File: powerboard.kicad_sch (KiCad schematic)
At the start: 24 parts, among them J1 B03B, J2 EMER_SW, J3 EMER_SW, Q1 TJ60S04M3L, U1 TLP222A

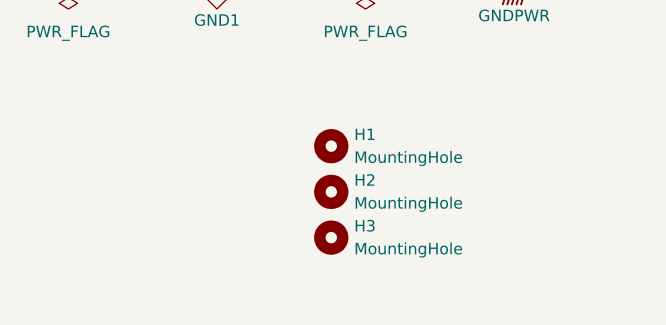
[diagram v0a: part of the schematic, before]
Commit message: pcb/sch: add a hole, silks
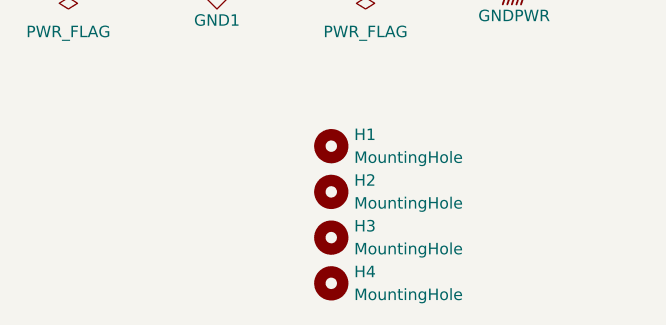
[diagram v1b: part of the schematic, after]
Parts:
- added H4: MountingHole, MountingHole:MountingHole_3.2mm_M3, symbol Mechanical:MountingHole
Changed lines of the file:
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@@
+	)
+	(symbol
+		(lib_id "Mechanical:MountingHole")
+		(at 248.92 100.33 0)
+		(unit 1)
+		(exclude_from_sim yes)
+		(in_bom no)
+		(on_board yes)
+		(dnp no)
+		(fields_autoplaced yes)
+		(property "Reference" "H4"
+			(at 251.46 99.0599 0)
+			(effects
+				(font
+					(size 1.27 1.27)
+				)
+				(justify left)
+			)
+		)
+		(property "Value" "MountingHole"
+			(at 251.46 101.5999 0)
+			(effects
+				(font
+					(size 1.27 1.27)
+				)
+				(justify left)
+			)
+		)
+		(property "Footprint" "MountingHole:MountingHole_3.2mm_M3"
+			(at 248.92 100.33 0)
+			(effects
+				(font
+					(size 1.27 1.27)
+				)
+				(hide yes)
+			)
+		)
+		(property "Datasheet" "~"
+			(at 248.92 100.33 0)
+			(effects
+				(font
+					(size 1.27 1.27)
+				)
+				(hide yes)
+			)
+		)
+		(property "Description" "Mounting Hole without connection"
+			(at 248.92 100.33 0)
+			(effects
+				(font
+					(size 1.27 1.27)
+				)
+				(hide yes)
+			)
+		)
+		(instances
+			(project "powerboard"
+				(path "/f61afb78-be8f-4a5f-ad16-61c0881e4198"
+					(reference "H4")
+					(unit 1)
+				)
+			)
+		)
 	)
 	(symbol

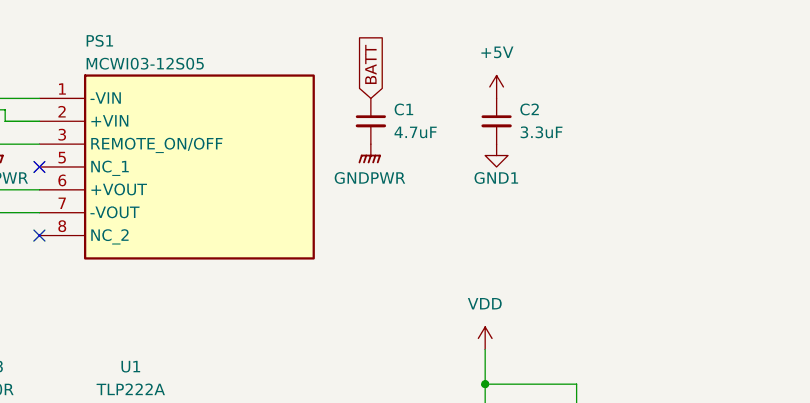
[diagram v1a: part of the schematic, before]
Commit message: sch: change Capacitance C1 (Power)
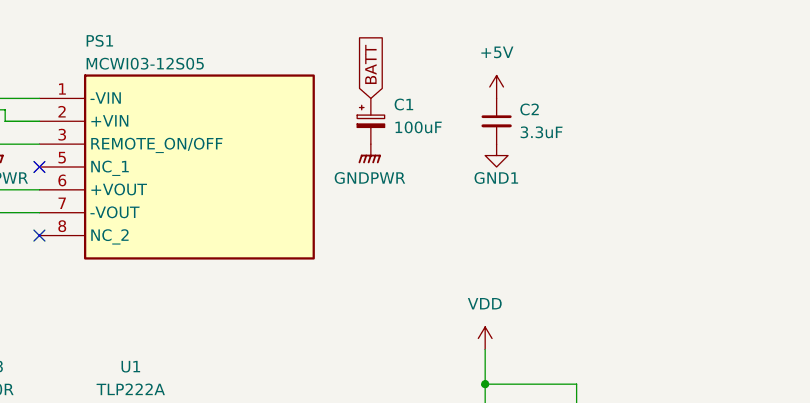
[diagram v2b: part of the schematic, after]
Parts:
- C1: value 4.7uF -> 100uF; footprint Capacitor_THT:C_Disc_D5.1mm_W3.2mm_P5.00mm -> Capacitor_THT:C_Radial_D5.0mm_H11.0mm_P2.00mm; symbol Device:C_Small -> Device:C_Polarized_Small
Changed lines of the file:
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@@
 	)
 	(symbol
-		(lib_id "Device:C_Small")
+		(lib_id "Device:C_Polarized_Small")
 		(at 132.08 36.83 0)
 		(unit 1)
@@
 		(fields_autoplaced yes)
 		(property "Reference" "C1"
-			(at 134.62 35.5662 0)
+			(at 134.62 35.0138 0)
 			(effects
 				(font
@@
 			)
 		)
-		(property "Value" "4.7uF"
-			(at 134.62 38.1062 0)
+		(property "Value" "100uF"
+			(at 134.62 37.5538 0)
 			(effects
 				(font
@@
 			)
 		)
-		(property "Footprint" "Capacitor_THT:C_Disc_D5.1mm_W3.2mm_P5.00mm"
+		(property "Footprint" "Capacitor_THT:C_Radial_D5.0mm_H11.0mm_P2.00mm"
 			(at 132.08 36.83 0)
 			(effects
@@
 			)
 		)
-		(property "Description" "Unpolarized capacitor, small symbol"
+		(property "Description" "Polarized capacitor, small symbol"
 			(at 132.08 36.83 0)
 			(effects

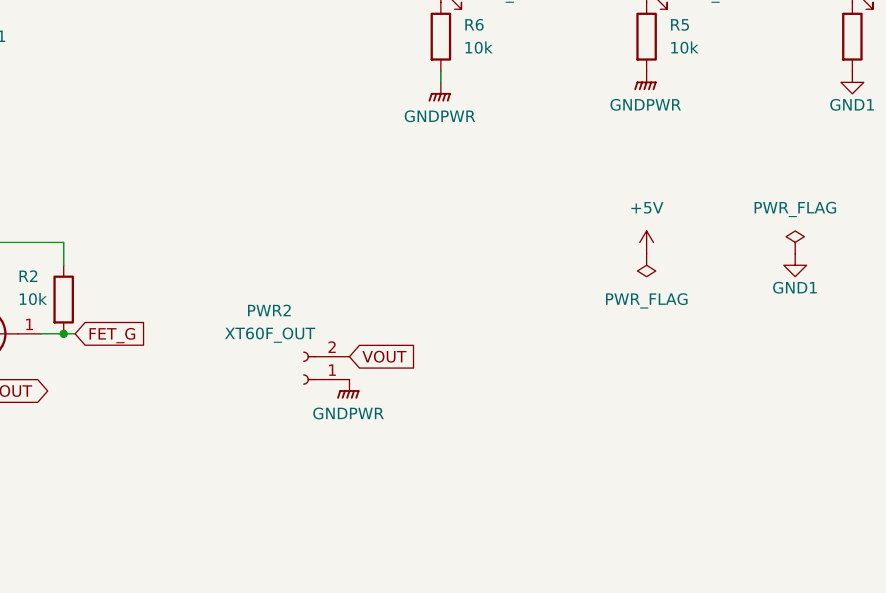
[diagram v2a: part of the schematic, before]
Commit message: pcb/sch: Add FET
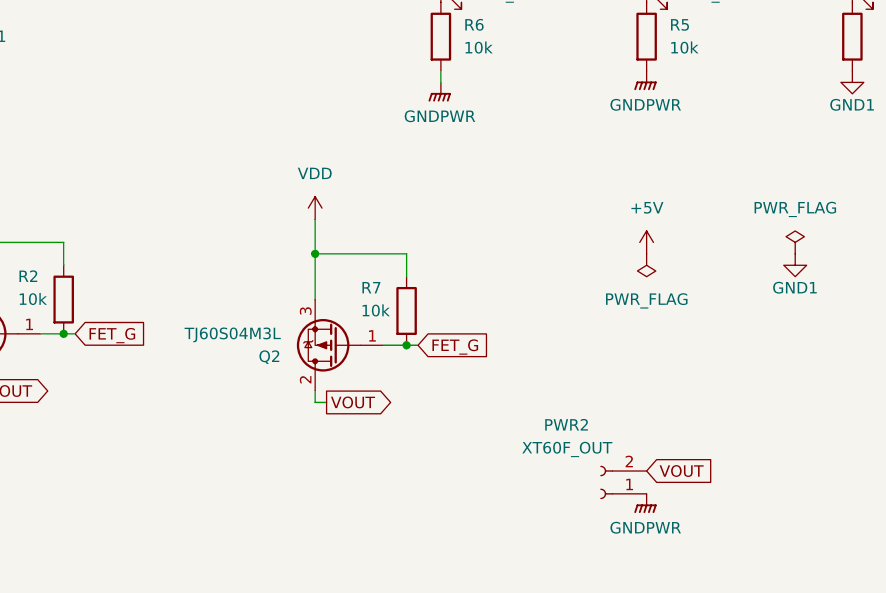
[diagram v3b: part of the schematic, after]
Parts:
- added Q2: TJ60S04M3L, Package_TO_SOT_SMD:TO-252-2, symbol Device:Q_PMOS_GDS
- added R7: 10k, Resistor_THT:R_Axial_DIN0207_L6.3mm_D2.5mm_P7.62mm_Horizontal, symbol Device:R
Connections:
- net FET_G: now also Q2.1 (G), R7.2
- net VDD: now also Q2.3 (S), R7.1
- net VOUT: now also Q2.2 (D)
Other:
- moved on the sheet: PWR2

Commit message: Revert "pcb/sch: Add FET"
This reverts commit 0032eebc1d6eb9ed2a957a3795ce5049efafd74e.
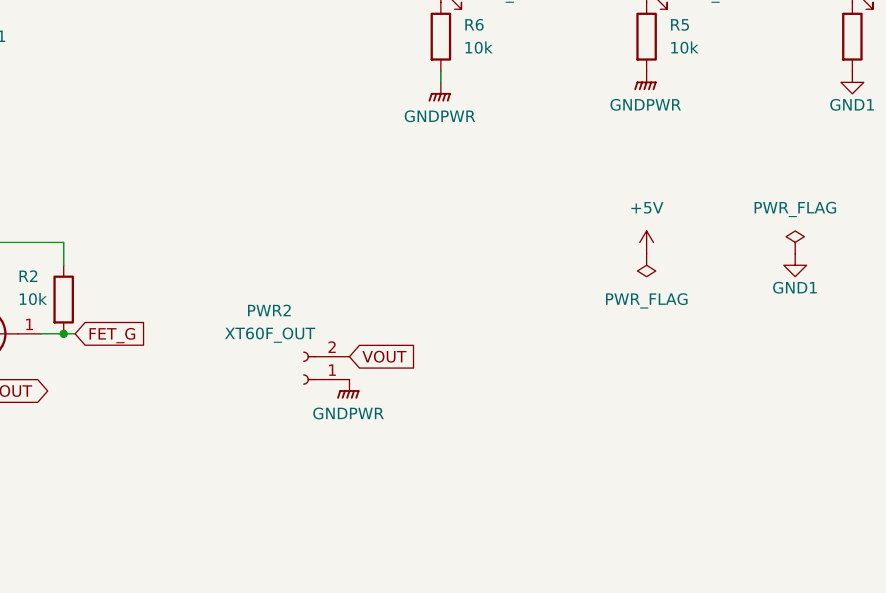
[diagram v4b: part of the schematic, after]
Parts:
- removed Q2: TJ60S04M3L, Package_TO_SOT_SMD:TO-252-2, symbol Device:Q_PMOS_GDS
- removed R7: 10k, Resistor_THT:R_Axial_DIN0207_L6.3mm_D2.5mm_P7.62mm_Horizontal, symbol Device:R
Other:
- moved on the sheet: PWR2

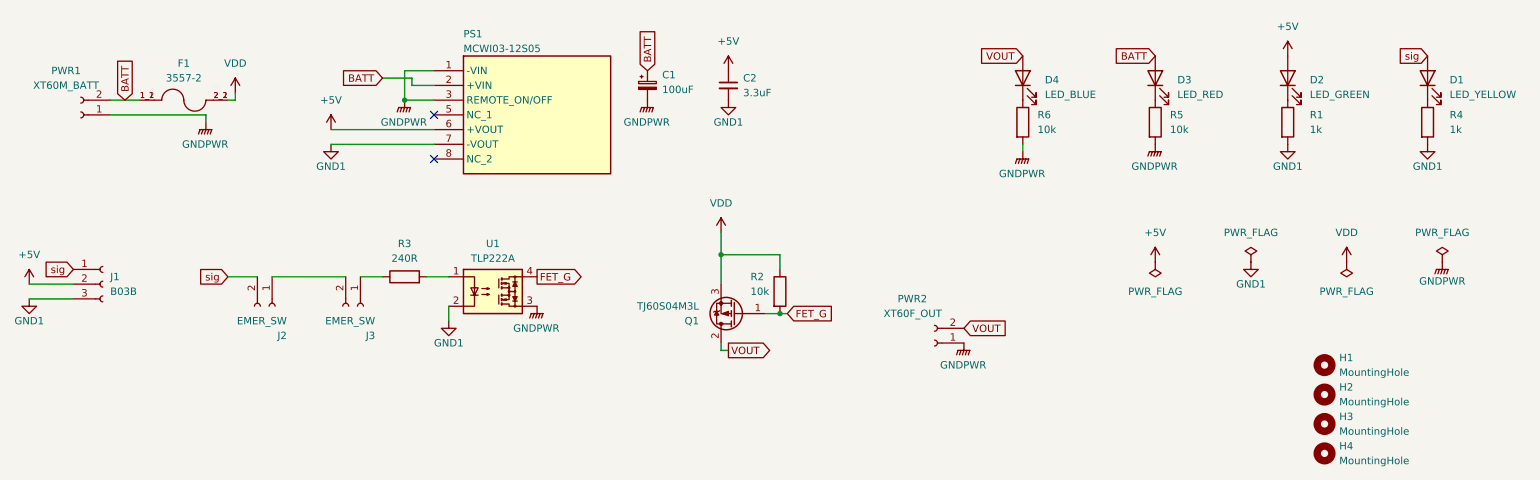
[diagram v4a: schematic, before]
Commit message: PCB: 分圧抵抗を追加、アノテーションをリセット
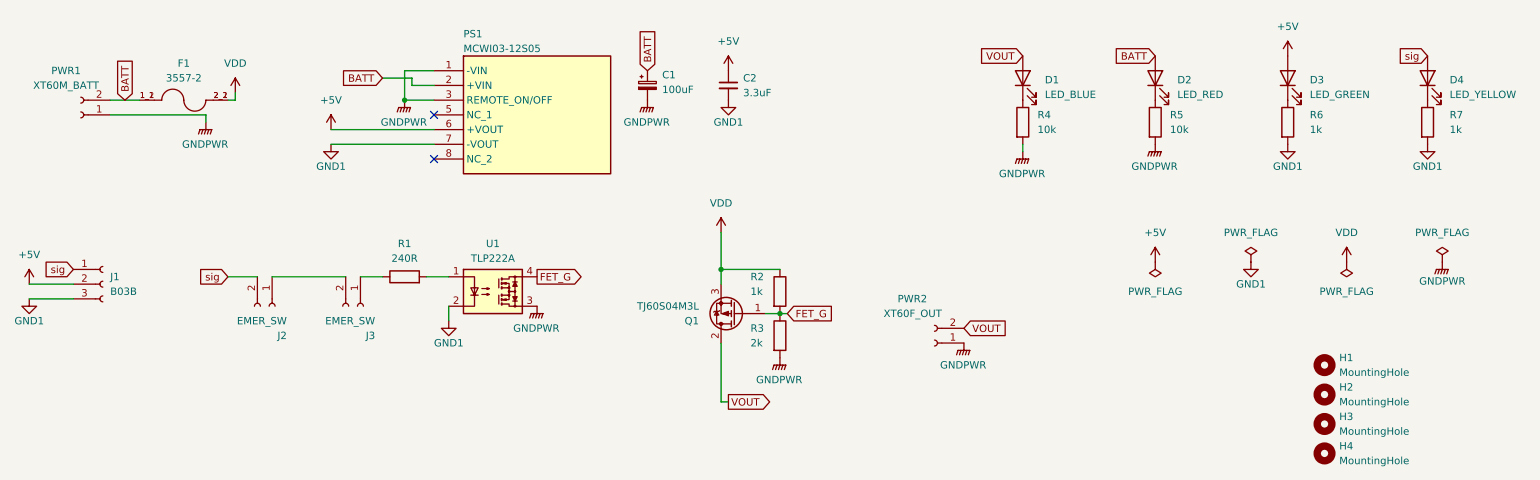
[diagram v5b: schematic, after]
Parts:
- added R3: 2k, symbol Device:R
- R2: value 10k -> 1k
- renumbered D4 to D1, D3 to D2, D2 to D3, D1 to D4, R3 to R1, R6 to R4, R1 to R6, R4 to R7
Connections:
- net FET_G: now also R3.1
- net GNDPWR: now also R3.2

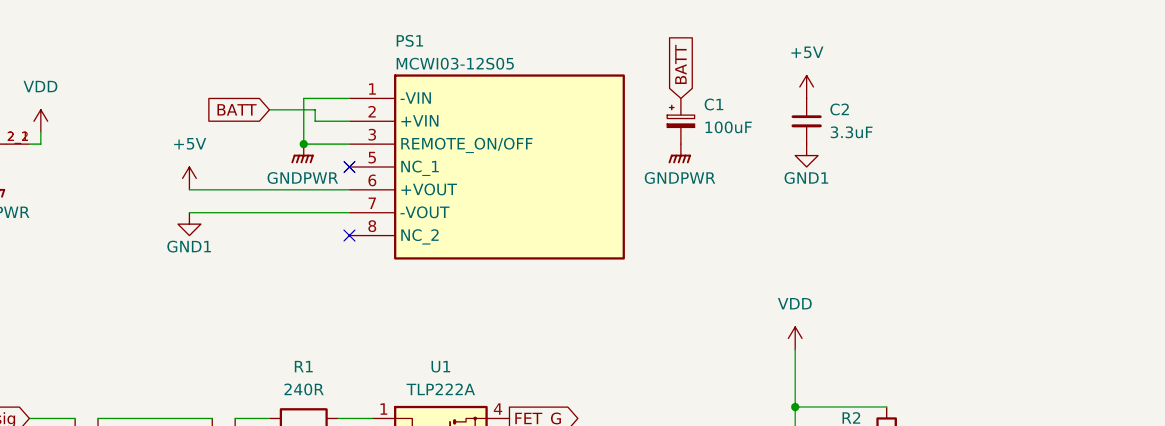
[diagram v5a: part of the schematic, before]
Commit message: PCB: DCDCを変更
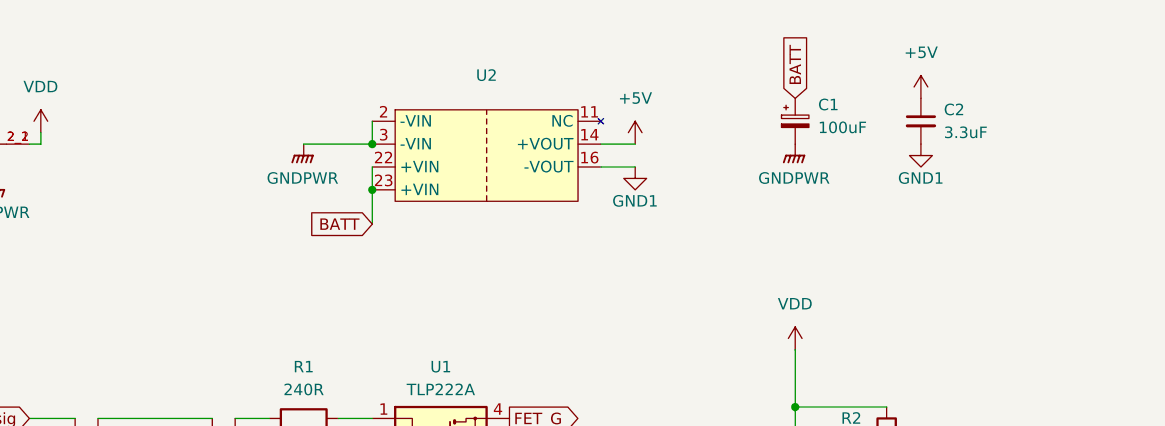
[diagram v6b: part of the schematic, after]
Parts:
- removed PS1: MCWI03-12S05, MCWI0312S05:MCWI0312S05, symbol MCWI03-12S05:MCWI03-12S05
- added U2: ~, symbol MIWI06-24S05:MIWI06-24S05
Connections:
- net +5V: now also U2.14 (+VOUT)
- net BATT: now also U2.22 (+VIN), U2.23 (+VIN)
- net GND1: now also U2.16 (-VOUT)
- net GNDPWR: now also U2.2 (-VIN), U2.3 (-VIN)
- no-connect marks 2 -> 0
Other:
- moved on the sheet: C1, C2

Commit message: PCB: DCDCの位置調整
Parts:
- added R4: 10k, Resistor_THT:R_Axial_DIN0207_L6.3mm_D2.5mm_P7.62mm_Horizontal, symbol Device:R
- R2: value 1k -> 10k
- R3: value 2k -> 10k; footprint (none) -> Resistor_THT:R_Axial_DIN0207_L6.3mm_D2.5mm_P7.62mm_Horizontal
- U1: renamed from U2; footprint (none) -> MIWI06-24S05:MIWI06-24S05
- renumbered R4 to R5, R5 to R6, R6 to R7, R7 to R8, U1 to U2
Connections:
- net GNDPWR: now also R4.2; no longer R3.2
- new net: R3.2, R4.1
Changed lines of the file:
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@@
 	(wire
 		(pts
-			(xy 144.78 91.44) (xy 144.78 81.28)
+			(xy 144.78 83.82) (xy 144.78 81.28)
 		)
 		(stroke
@@
 	(wire
 		(pts
-			(xy 146.05 91.44) (xy 144.78 91.44)
+			(xy 143.51 83.82) (xy 144.78 83.82)
 		)
 		(stroke
@@
 	(global_label "VOUT"
 		(shape output)
-		(at 146.05 91.44 0)
+		(at 143.51 83.82 180)
 		(fields_autoplaced yes)
 		(effects
@@
 				(size 1.27 1.27)
 			)
-			(justify left)
+			(justify right)
 		)
 		(property "Intersheetrefs" "${INTERSHEET_REFS}"
-			(at 153.7524 91.44 0)
+			(at 135.8076 83.82 0)
 			(effects
 				(font
 					(size 1.27 1.27)
 				)
-				(justify left)
+				(justify right)
 				(hide yes)
 			)
@@
 	(symbol
 		(lib_id "power:GNDPWR")
-		(at 154.94 83.82 0)
+		(at 154.94 91.44 0)
 		(unit 1)
 		(exclude_from_sim no)
@@
 		(dnp no)
 		(fields_autoplaced yes)
-		(property "Reference" "#PWR014"
-			(at 154.94 88.9 0)
+		(property "Reference" "#PWR012"
+			(at 154.94 96.52 0)
 			(effects
 				(font
@@
 		)
 		(property "Value" "GNDPWR"
-			(at 154.813 87.63 0)
+			(at 154.813 95.25 0)
 			(effects
 				(font
@@
 		)
 		(property "Footprint" ""
-			(at 154.94 85.09 0)
+			(at 154.94 92.71 0)
 			(effects
 				(font
@@
 		)
 		(property "Datasheet" ""
-			(at 154.94 85.09 0)
+			(at 154.94 92.71 0)
 			(effects
 				(font
@@
 		)
 		(property "Description" "Power symbol creates a global label with name \"GNDPWR\" , global ground"
-			(at 154.94 83.82 0)
+			(at 154.94 91.44 0)
 			(effects
 				(font
@@
 			(project "powerboard"
 				(path "/f61afb78-be8f-4a5f-ad16-61c0881e4198"
-					(reference "#PWR014")
+					(reference "#PWR012")
 					(unit 1)
 				)
@@
 		(on_board yes)
 		(dnp no)
-		(property "Reference" "R7"
+		(property "Reference" "R8"
 			(at 270.51 41.91 0)
 			(effects
@@
 			(project "powerboard"
 				(path "/f61afb78-be8f-4a5f-ad16-61c0881e4198"
-					(reference "R7")
+					(reference "R8")
 					(unit 1)
 				)
@@
 		(dnp no)
 		(fields_autoplaced yes)
-		(property "Reference" "R5"
+		(property "Reference" "R6"
 			(at 222.25 41.9099 0)
 			(effects
@@
 			(project "powerboard"
 				(path "/f61afb78-be8f-4a5f-ad16-61c0881e4198"
-					(reference "R5")
+					(reference "R6")
 					(unit 1)
 				)
@@
 		(dnp no)
 		(fields_autoplaced yes)
-		(property "Reference" "R4"
+		(property "Reference" "R5"
 			(at 199.39 41.9099 0)
 			(effects
@@
 			(project "powerboard"
 				(path "/f61afb78-be8f-4a5f-ad16-61c0881e4198"
-					(reference "R4")
+					(reference "R5")
 					(unit 1)
 				)
@@
 		(on_board yes)
 		(dnp no)
-		(property "Reference" "#PWR013"
+		(property "Reference" "#PWR014"
 			(at 158.75 45.72 0)
 			(effects
@@
 			(project "powerboard"
 				(path "/f61afb78-be8f-4a5f-ad16-61c0881e4198"
-					(reference "#PWR013")
+					(reference "#PWR014")
 					(unit 1)
 				)
@@
 		(on_board yes)
 		(dnp no)
-		(property "Reference" "R6"
+		(property "Reference" "R7"
 			(at 246.38 41.91 0)
 			(effects
@@
 			(project "powerboard"
 				(path "/f61afb78-be8f-4a5f-ad16-61c0881e4198"
-					(reference "R6")
+					(reference "R7")
 					(unit 1)
 				)
@@
 		(dnp no)
 		(fields_autoplaced yes)
-		(property "Reference" "#PWR012"
+		(property "Reference" "#PWR013"
 			(at 158.75 38.1 0)
 			(effects
@@
 			(project "powerboard"
 				(path "/f61afb78-be8f-4a5f-ad16-61c0881e4198"
-					(reference "#PWR012")
+					(reference "#PWR013")
 					(unit 1)
 				)
@@
 	)
 	(symbol
+		(lib_id "Device:R")
+		(at 154.94 87.63 0)
+		(unit 1)
+		(exclude_from_sim no)
+		(in_bom yes)
+		(on_board yes)
+		(dnp no)
+		(property "Reference" "R4"
+			(at 149.86 86.36 0)
+			(effects
+				(font
+					(size 1.27 1.27)
+				)
+				(justify left)
+			)
+		)
+		(property "Value" "10k"
+			(at 149.86 88.9 0)
+			(effects
+				(font
+					(size 1.27 1.27)
+				)
+				(justify left)
+			)
+		)
+		(property "Footprint" "Resistor_THT:R_Axial_DIN0207_L6.3mm_D2.5mm_P7.62mm_Horizontal"
+			(at 153.162 87.63 90)
+			(effects
+				(font
+					(size 1.27 1.27)
+				)
+				(hide yes)
+			)
+		)
+		(property "Datasheet" "~"
+			(at 154.94 87.63 0)
+			(effects
+				(font
+					(size 1.27 1.27)
+				)
+				(hide yes)
+			)
+		)
+		(property "Description" "Resistor"
+			(at 154.94 87.63 0)
+			(effects
+				(font
+					(size 1.27 1.27)
+				)
+				(hide yes)
+			)
+		)
+		(pin "1"
+		)
+		(pin "2"
+		)
+		(instances
+			(project "powerboard"
+				(path "/f61afb78-be8f-4a5f-ad16-61c0881e4198"
+					(reference "R4")
+					(unit 1)
+				)
+			)
+		)
+	)
+	(symbol
 		(lib_id "power:GNDPWR")
 		(at 90.17 39.37 0)
@@
 		(dnp no)
 		(fields_autoplaced yes)
-		(property "Reference" "#PWR07"
+		(property "Reference" "#PWR05"
 			(at 90.17 44.45 0)
 			(effects
@@
 			(project "powerboard"
 				(path "/f61afb78-be8f-4a5f-ad16-61c0881e4198"
-					(reference "#PWR07")
+					(reference "#PWR05")
 					(unit 1)
 				)
@@
 		(on_board yes)
 		(dnp no)
-		(property "Reference" "#PWR08"
+		(property "Reference" "#PWR06"
 			(at 97.79 83.82 0)
 			(effects
@@
 			(project "powerboard"
 				(path "/f61afb78-be8f-4a5f-ad16-61c0881e4198"
-					(reference "#PWR08")
+					(reference "#PWR06")
 					(unit 1)
 				)
@@
 		(dnp no)
 		(fields_autoplaced yes)
-		(property "Reference" "U2"
+		(property "Reference" "U1"
 			(at 110.49 31.75 0)
 			(effects
@@
 			)
 		)
-		(property "Footprint" ""
+		(property "Footprint" "MIWI06-24S05:MIWI06-24S05"
 			(at 97.79 36.83 0)
 			(effects
@@
 			(project "powerboard"
 				(path "/f61afb78-be8f-4a5f-ad16-61c0881e4198"
-					(reference "U2")
+					(reference "U1")
 					(unit 1)
 				)
@@
 		(dnp no)
 		(fields_autoplaced yes)
-		(property "Reference" "#PWR09"
+		(property "Reference" "#PWR07"
 			(at 113.03 80.01 0)
 			(effects
@@
 			(project "powerboard"
 				(path "/f61afb78-be8f-4a5f-ad16-61c0881e4198"
-					(reference "#PWR09")
+					(reference "#PWR07")
 					(unit 1)
 				)
@@
 			)
 		)
-		(property "Value" "2k"
+		(property "Value" "10k"
 			(at 149.86 81.28 0)
 			(effects
@@
 			)
 		)
-		(property "Footprint" ""
+		(property "Footprint" "Resistor_THT:R_Axial_DIN0207_L6.3mm_D2.5mm_P7.62mm_Horizontal"
 			(at 153.162 80.01 90)
 			(effects
@@
 			)
 		)
-		(property "Value" "1k"
+		(property "Value" "10k"
 			(at 149.86 72.39 0)
 			(effects
@@
 		(on_board yes)
 		(dnp no)
-		(property "Reference" "#PWR06"
+		(property "Reference" "#PWR09"
 			(at 127 48.26 0)
 			(effects
@@
 			(project "powerboard"
 				(path "/f61afb78-be8f-4a5f-ad16-61c0881e4198"
-					(reference "#PWR06")
+					(reference "#PWR09")
 					(unit 1)
 				)
@@
 		(dnp no)
 		(fields_autoplaced yes)
-		(property "Reference" "U1"
+		(property "Reference" "U2"
 			(at 105.41 64.135 0)
 			(effects
@@
 			(project "powerboard"
 				(path "/f61afb78-be8f-4a5f-ad16-61c0881e4198"
-					(reference "U1")
+					(reference "U2")
 					(unit 1)
 				)
@@
 		(dnp no)
 		(fields_autoplaced yes)
-		(property "Reference" "#PWR05"
+		(property "Reference" "#PWR08"
 			(at 127 43.18 0)
 			(effects
@@
 			(project "powerboard"
 				(path "/f61afb78-be8f-4a5f-ad16-61c0881e4198"
-					(reference "#PWR05")
+					(reference "#PWR08")
 					(unit 1)
 				)

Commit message: INITIAL COMMIT
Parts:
- removed U1: ~, MIWI06-24S05:MIWI06-24S05, symbol MIWI06-24S05:MIWI06-24S05
- added U1: PQQ10W-Q24-S5-S, PQQ10W-Q24-S5-S:CONV_PQQ10W-Q24-S5-S, symbol PQQ10W-Q24-S5-S:PQQ10W-Q24-S5-S
- C1: value 100uF -> 47uF
- C2: value 3.3uF -> 22uF; footprint Capacitor_THT:C_Disc_D5.1mm_W3.2mm_P5.00mm -> Capacitor_THT:C_Radial_D5.0mm_H11.0mm_P2.00mm; symbol Device:C_Small -> Device:C_Polarized_Small
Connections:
- net +5V: now also U1.6 (+VO)
- net BATT: now also U1.2 (VIN)
- net GND1: now also U1.7 (0V)
- net GNDPWR: now also U1.1 (GND)
- no-connect marks 0 -> 1
